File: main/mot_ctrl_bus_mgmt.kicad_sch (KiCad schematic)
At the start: 20 parts, among them Q1401 Q_NMOS_GDS, U1401 74LS08

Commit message: Updates
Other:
- note added: "The motor control is modulated by the power PWM. The low phase is prefered as it will allow the driver charge pump to load. If the feature can be implemented in software, the AND gate can be removed and bypassed."
- note removed: "The motor control is modulated by the power PWM. The low phase is prefered as it will allow the driver charge pump to load. If the feature can be implemented in software, the AND gate can be bypassed."
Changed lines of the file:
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@@
 		)
 	)
-	(text "The motor control is modulated by the power PWM.\nThe low phase is prefered as it will allow the driver charge pump to load.\nIf the feature can be implemented in software, the AND gate can be bypassed."
+	(text "The motor control is modulated by the power PWM.\nThe low phase is prefered as it will allow the driver charge pump to load.\nIf the feature can be implemented in software, the AND gate can be removed and bypassed."
 		(exclude_from_sim no)
 		(at 25.908 71.628 0)
@@
 	(label "MOT_CTRL.BH"
 		(at 147.32 125.73 180)
+		(fields_autoplaced yes)
 		(effects
 			(font
@@
 	(label "MOT_CTRL.CH"
 		(at 147.32 151.13 180)
+		(fields_autoplaced yes)
 		(effects
 			(font
@@
 	(label "MOT_DRIVE.AL"
 		(at 83.82 97.79 180)
+		(fields_autoplaced yes)
 		(effects
 			(font
@@
 	(label "MOT_CTRL.AL"
 		(at 113.03 93.98 0)
+		(fields_autoplaced yes)
 		(effects
 			(font
@@
 	(label "MOT_CTRL.AH"
 		(at 147.32 100.33 180)
+		(fields_autoplaced yes)
 		(effects
 			(font
@@
 	(label "MOT_DRIVE.CL"
 		(at 83.82 148.59 180)
+		(fields_autoplaced yes)
 		(effects
 			(font
@@
 	(label "MOT_DRIVE.BH"
 		(at 158.75 125.73 0)
+		(fields_autoplaced yes)
 		(effects
 			(font
@@
 	(label "MOT_DRIVE.AH"
 		(at 158.75 100.33 0)
+		(fields_autoplaced yes)
 		(effects
 			(font
@@
 	(label "MOT_DRIVE.BL"
 		(at 83.82 123.19 180)
+		(fields_autoplaced yes)
 		(effects
 			(font
@@
 	(label "MOT_CTRL.BL"
 		(at 113.03 119.38 0)
+		(fields_autoplaced yes)
 		(effects
 			(font
@@
 	(label "MOT_DRIVE.CH"
 		(at 158.75 151.13 0)
+		(fields_autoplaced yes)
 		(effects
 			(font
@@
 	(label "MOT_CTRL.CL"
 		(at 113.03 144.78 0)
+		(fields_autoplaced yes)
 		(effects
 			(font

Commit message: Finalize sch and start component mapping
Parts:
- C1401: footprint (none) -> Capacitor_SMD:C_0805_2012Metric
- D1401, D1402, D1403, D1404, D1405, D1406: footprint (none) -> LED_SMD:LED_0805_2012Metric
- JP1101: renamed from JP1204; footprint (none) -> Jumper:SolderJumper-2_P1.3mm_Open_TrianglePad1.0x1.5mm
- JP1103: renamed from JP1201; footprint (none) -> Jumper:SolderJumper-3_P2.0mm_Open_TrianglePad1.0x1.5mm
- JP1104: renamed from JP1202; footprint (none) -> Jumper:SolderJumper-3_P2.0mm_Open_TrianglePad1.0x1.5mm
- JP1402: renamed from JP1502; footprint (none) -> Jumper:SolderJumper-3_P2.0mm_Open_TrianglePad1.0x1.5mm
- R1401, R1402, R1403, R1404, R1405, R1406, R1407: footprint (none) -> Resistor_SMD:R_0805_2012Metric

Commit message: update BOM
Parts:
- U1401: footprint (none) -> Package_DFN_QFN:DHVQFN-14-1EP_2.5x3mm_P0.5mm_EP1x1.5mm; MPN (none) -> 74LVC08ABQ,115
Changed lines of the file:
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@@
 	)
 	(symbol
+		(lib_name "74LS08_2")
 		(lib_id "74xx:74LS08")
 		(at 99.06 100.33 0)
@@
 			)
 		)
-		(property "Footprint" ""
+		(property "Footprint" "Package_DFN_QFN:DHVQFN-14-1EP_2.5x3mm_P0.5mm_EP1x1.5mm"
 			(at 99.06 100.33 0)
 			(effects
@@
 		)
 		(property "Description" "Quad And2"
+			(at 99.06 100.33 0)
+			(effects
+				(font
+					(size 1.27 1.27)
+				)
+				(hide yes)
+			)
+		)
+		(property "MPN" "74LVC08ABQ,115"
 			(at 99.06 100.33 0)
 			(effects
@@
 			)
 		)
-		(property "Footprint" ""
+		(property "Footprint" "Package_DFN_QFN:DHVQFN-14-1EP_2.5x3mm_P0.5mm_EP1x1.5mm"
 			(at 99.06 45.72 0)
 			(effects
@@
 		)
 		(property "Description" "Quad And2"
+			(at 99.06 45.72 0)
+			(effects
+				(font
+					(size 1.27 1.27)
+				)
+				(hide yes)
+			)
+		)
+		(property "MPN" "74LVC08ABQ,115"
 			(at 99.06 45.72 0)
 			(effects
@@
 			)
 		)
-		(property "Footprint" ""
+		(property "Footprint" "Package_DFN_QFN:DHVQFN-14-1EP_2.5x3mm_P0.5mm_EP1x1.5mm"
 			(at 99.06 151.13 0)
 			(effects
@@
 		)
 		(property "Description" "Quad And2"
+			(at 99.06 151.13 0)
+			(effects
+				(font
+					(size 1.27 1.27)
+				)
+				(hide yes)
+			)
+		)
+		(property "MPN" "74LVC08ABQ,115"
 			(at 99.06 151.13 0)
 			(effects
@@
 			)
 		)
-		(property "Footprint" ""
+		(property "Footprint" "Package_DFN_QFN:DHVQFN-14-1EP_2.5x3mm_P0.5mm_EP1x1.5mm"
 			(at 99.06 171.45 0)
 			(effects
@@
 		)
 		(property "Description" "Quad And2"
+			(at 99.06 171.45 0)
+			(effects
+				(font
+					(size 1.27 1.27)
+				)
+				(hide yes)
+			)
+		)
+		(property "MPN" "74LVC08ABQ,115"
 			(at 99.06 171.45 0)
 			(effects
@@
 	)
 	(symbol
+		(lib_name "74LS08_1")
 		(lib_id "74xx:74LS08")
 		(at 99.06 125.73 0)
@@
 			)
 		)
-		(property "Footprint" ""
+		(property "Footprint" "Package_DFN_QFN:DHVQFN-14-1EP_2.5x3mm_P0.5mm_EP1x1.5mm"
 			(at 99.06 125.73 0)
 			(effects
@@
 			(at 99.06 125.73 0)
 			(effects
+				(font
+					(size 1.27 1.27)
+				)
+				(hide yes)
+			)
+		)
+		(property "MPN" "74LVC08ABQ,115"
+			(at 99.06 125.73 0)
+			(effects

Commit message: BOM OK
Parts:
- removed Q1401: Q_NMOS_GDS, symbol Device:Q_NMOS_GDS
- added Q1101: IRLML0030, Package_TO_SOT_SMD:SOT-23, symbol Transistor_FET:IRLML0030
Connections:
- net GNDD: now also Q1101.2 (S)
- net LED_EN: now also Q1101.1 (G)
- net at D1401.1 (K), D1402.1 (K), D1403.1 (K)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: now also Q1101.3 (D)
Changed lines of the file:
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@@
-	)
-	(symbol
-		(lib_id "Device:Q_NMOS_GDS")
-		(at 264.16 76.2 0)
-		(unit 1)
-		(exclude_from_sim no)
-		(in_bom yes)
-		(on_board yes)
-		(dnp no)
-		(fields_autoplaced yes)
-		(property "Reference" "Q1401"
-			(at 270.51 74.9299 0)
-			(effects
-				(font
-					(size 1.27 1.27)
-				)
-				(justify left)
-			)
-		)
-		(property "Value" "Q_NMOS_GDS"
-			(at 270.51 77.4699 0)
-			(effects
-				(font
-					(size 1.27 1.27)
-				)
-				(justify left)
-			)
-		)
-		(property "Footprint" ""
-			(at 269.24 73.66 0)
-			(effects
-				(font
-					(size 1.27 1.27)
-				)
-				(hide yes)
-			)
-		)
-		(property "Datasheet" "~"
-			(at 264.16 76.2 0)
-			(effects
-				(font
-					(size 1.27 1.27)
-				)
-				(hide yes)
-			)
-		)
-		(property "Description" "N-MOSFET transistor, gate/drain/source"
-			(at 264.16 76.2 0)
-			(effects
-				(font
-					(size 1.27 1.27)
-				)
-				(hide yes)
-			)
-		)
-		(pin "2"
-		)
-		(pin "3"
-		)
-		(pin "1"
-		)
-		(instances
-			(project "dsv4"
-				(path "/c07e9297-fde8-4755-803e-d05072cd6096/0865f076-bf0e-442f-8617-d4097538e68b/e313533d-7862-466d-aec4-d9675212cabe"
-					(reference "Q1401")
-					(unit 1)
-				)
-				(path "/c07e9297-fde8-4755-803e-d05072cd6096/0865f076-bf0e-442f-8617-d4097538e68b/2d15f287-a464-4822-9e76-d4ca4cb9f82a"
-					(reference "Q1101")
-					(unit 1)
-				)
-			)
-		)
 	)
 	(symbol
@@
 					(unit 1)
 				)
+			)
+		)
+	)
+	(symbol
+		(lib_id "Transistor_FET:IRLML0030")
+		(at 264.16 76.2 0)
+		(unit 1)
+		(exclude_from_sim no)
+		(in_bom yes)
+		(on_board yes)
+		(dnp no)
+		(fields_autoplaced yes)
+		(property "Reference" "Q1101"
+			(at 270.51 74.9299 0)
+			(effects
+				(font
+					(size 1.27 1.27)
+				)
+				(justify left)
+			)
+		)
+		(property "Value" "IRLML0030"
+			(at 270.51 77.4699 0)
+			(effects
+				(font
+					(size 1.27 1.27)
+				)
+				(justify left)
+			)
+		)
+		(property "Footprint" "Package_TO_SOT_SMD:SOT-23"
+			(at 269.24 78.105 0)
+			(effects
+				(font
+					(size 1.27 1.27)
+					(italic yes)
+				)
+				(justify left)
+				(hide yes)
+			)
+		)
+		(property "Datasheet" "https://www.infineon.com/dgdl/irlml0030pbf.pdf?fileId=5546d462533600a401535664773825df"
+			(at 269.24 80.01 0)
+			(effects
+				(font
+					(size 1.27 1.27)
+				)
+				(justify left)
+				(hide yes)
+			)
+		)
+		(property "Description" "5.3A Id, 30V Vds, 27mOhm Rds, N-Channel HEXFET Power MOSFET, SOT-23"
+			(at 264.16 76.2 0)
+			(effects
+				(font
+					(size 1.27 1.27)
+				)
+				(hide yes)
+			)
+		)
+		(pin "1"
+		)
+		(pin "3"
+		)
+		(pin "2"
+		)
+		(instances
+			(project "dsv4"
+				(path "/c07e9297-fde8-4755-803e-d05072cd6096/0865f076-bf0e-442f-8617-d4097538e68b/2d15f287-a464-4822-9e76-d4ca4cb9f82a"
+					(reference "Q1101")
+					(unit 1)
+				)
+				(path "/c07e9297-fde8-4755-803e-d05072cd6096/0865f076-bf0e-442f-8617-d4097538e68b/e313533d-7862-466d-aec4-d9675212cabe"
+					(reference "Q1401")
+					(unit 1)
+				)

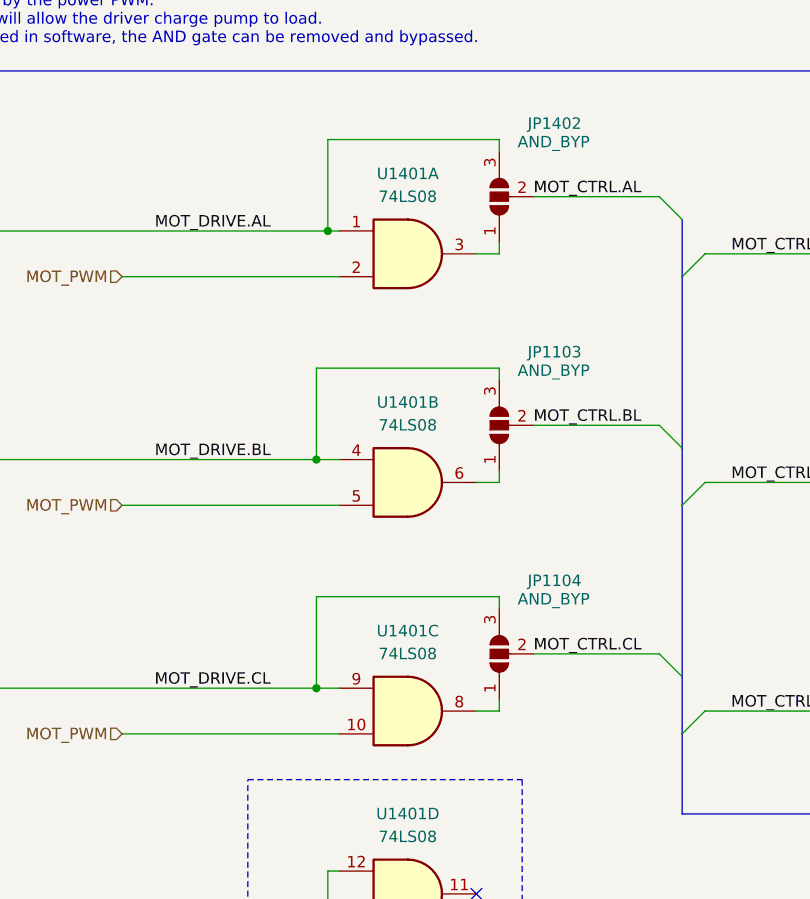
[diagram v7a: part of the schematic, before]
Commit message: Power routed
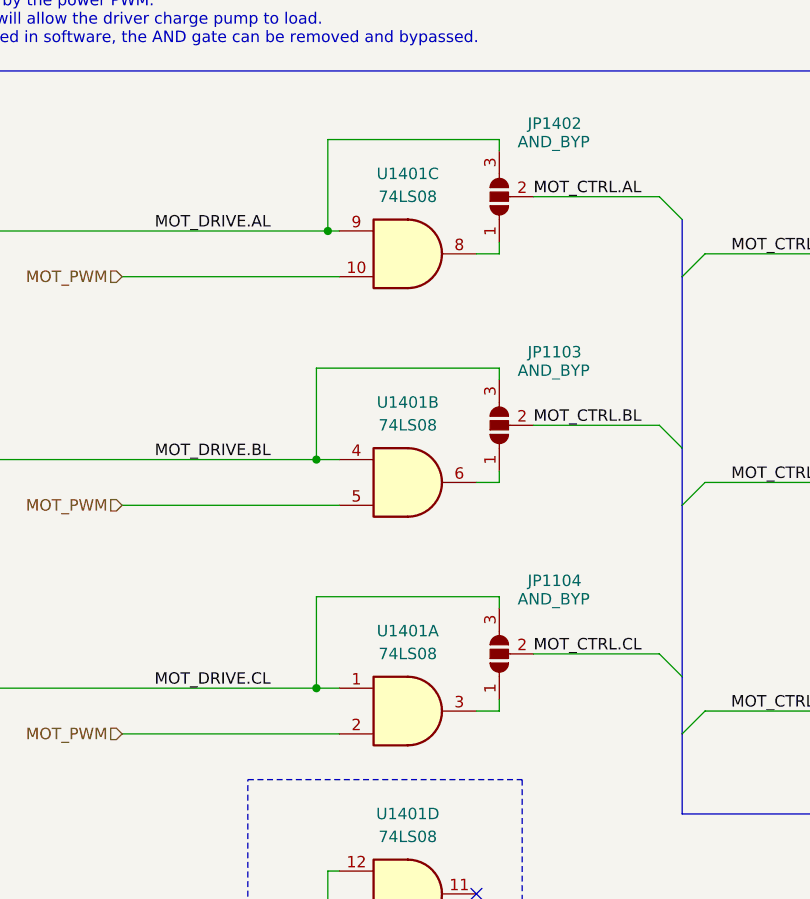
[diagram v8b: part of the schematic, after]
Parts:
- U1401: footprint Package_DFN_QFN:DHVQFN-14-1EP_2.5x3mm_P0.5mm_EP1x1.5mm -> Package_SO:TSSOP-14_4.4x5mm_P0.65mm
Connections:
- net MOT_DRIVE.AL: now also U1401.9; no longer U1401.1
- net MOT_DRIVE.CL: now also U1401.1; no longer U1401.9
- net at U1401.3: now also JP1104.1 (A); no longer JP1402.1 (A)
- net at U1401.8: now also JP1402.1 (A); no longer JP1104.1 (A)
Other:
- moved on the sheet: U1401A, U1401C
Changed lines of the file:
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@@
 		(comment 1 "Defis solaires 2024")
 	)
+	(rectangle
+		(start 81.28 158.75)
+		(end 111.76 186.69)
+		(stroke
+			(width 0)
+			(type dash)
+		)
+		(fill
+			(type none)
+		)
+	)
+	(text "Any high value to avoid floating gate\nwhile not wasting power."
+		(exclude_from_sim no)
+		(at 247.904 82.55 0)
+		(effects
+			(font
+				(size 1.27 1.27)
+			)
+			(justify right bottom)
+		)
+	)
+	(text "Unused"
+		(exclude_from_sim no)
+		(at 111.252 186.182 0)
+		(effects
+			(font
+				(size 1.27 1.27)
+			)
+			(justify right bottom)
+		)
+	)
+	(text "The motor control is modulated by the power PWM.\nThe low phase is prefered as it will allow the driver charge pump to load.\nIf the feature can be implemented in software, the AND gate can be removed and bypassed."
+		(exclude_from_sim no)
+		(at 25.908 71.628 0)
+		(effects
+			(font
+				(size 1.27 1.27)
+			)
+			(justify left top)
+		)
+	)
 	(junction
 		(at 50.8 80.01)
@@
 		)
 	)
-	(rectangle
-		(start 81.28 158.75)
-		(end 111.76 186.69)
-		(stroke
-			(width 0)
-			(type dash)
-		)
-		(fill
-			(type none)
-		)
-	)
-	(text "Any high value to avoid floating gate\nwhile not wasting power."
-		(exclude_from_sim no)
-		(at 247.904 82.55 0)
-		(effects
-			(font
-				(size 1.27 1.27)
-			)
-			(justify right bottom)
-		)
-	)
-	(text "Unused"
-		(exclude_from_sim no)
-		(at 111.252 186.182 0)
-		(effects
-			(font
-				(size 1.27 1.27)
-			)
-			(justify right bottom)
-		)
-	)
-	(text "The motor control is modulated by the power PWM.\nThe low phase is prefered as it will allow the driver charge pump to load.\nIf the feature can be implemented in software, the AND gate can be removed and bypassed."
-		(exclude_from_sim no)
-		(at 25.908 71.628 0)
-		(effects
-			(font
-				(size 1.27 1.27)
-			)
-			(justify left top)
-		)
-	)
 	(label "MOT_CTRL.BH"
 		(at 147.32 125.73 180)
@@
 		(lib_name "74LS08_2")
 		(lib_id "74xx:74LS08")
-		(at 99.06 100.33 0)
+		(at 99.06 151.13 0)
 		(unit 1)
 		(exclude_from_sim no)
@@
 		(fields_autoplaced yes)
 		(property "Reference" "U1401"
-			(at 99.0517 91.44 0)
+			(at 99.0517 142.24 0)
 			(effects
 				(font
@@
 		)
 		(property "Value" "74LS08"
-			(at 99.0517 93.98 0)
+			(at 99.0517 144.78 0)
 			(effects
 				(font
@@
 			)
 		)
-		(property "Footprint" "Package_DFN_QFN:DHVQFN-14-1EP_2.5x3mm_P0.5mm_EP1x1.5mm"
-			(at 99.06 100.33 0)
+		(property "Footprint" "Package_SO:TSSOP-14_4.4x5mm_P0.65mm"
+			(at 99.06 151.13 0)
 			(effects
 				(font
@@
 		)
 		(property "Datasheet" "http://www.ti.com/lit/gpn/sn74LS08"
-			(at 99.06 100.33 0)
+			(at 99.06 151.13 0)
 			(effects
 				(font
@@
 		)
 		(property "Description" "Quad And2"
-			(at 99.06 100.33 0)
+			(at 99.06 151.13 0)
 			(effects
 				(font
@@
 		)
 		(property "MPN" "74LVC08ABQ,115"
-			(at 99.06 100.33 0)
+			(at 99.06 151.13 0)
 			(effects
 				(font
@@
 			)
 		)
-		(property "Footprint" "Package_DFN_QFN:DHVQFN-14-1EP_2.5x3mm_P0.5mm_EP1x1.5mm"
+		(property "Footprint" "Package_SO:TSSOP-14_4.4x5mm_P0.65mm"
 			(at 99.06 45.72 0)
 			(effects
@@
 	(symbol
 		(lib_id "74xx:74LS08")
-		(at 99.06 151.13 0)
+		(at 99.06 100.33 0)
 		(unit 3)
 		(exclude_from_sim no)
@@
 		(fields_autoplaced yes)
 		(property "Reference" "U1401"
-			(at 99.0517 142.24 0)
+			(at 99.0517 91.44 0)
 			(effects
 				(font
@@
 		)
 		(property "Value" "74LS08"
-			(at 99.0517 144.78 0)
+			(at 99.0517 93.98 0)
 			(effects
 				(font
@@
 			)
 		)
-		(property "Footprint" "Package_DFN_QFN:DHVQFN-14-1EP_2.5x3mm_P0.5mm_EP1x1.5mm"
-			(at 99.06 151.13 0)
+		(property "Footprint" "Package_SO:TSSOP-14_4.4x5mm_P0.65mm"
+			(at 99.06 100.33 0)
 			(effects
 				(font
@@
 		)
 		(property "Datasheet" "http://www.ti.com/lit/gpn/sn74LS08"
-			(at 99.06 151.13 0)
+			(at 99.06 100.33 0)
 			(effects
 				(font
@@
 		)
 		(property "Description" "Quad And2"
-			(at 99.06 151.13 0)
+			(at 99.06 100.33 0)
 			(effects
 				(font
@@
 		)
 		(property "MPN" "74LVC08ABQ,115"
-			(at 99.06 151.13 0)
+			(at 99.06 100.33 0)
 			(effects
 				(font
@@
 			)
 		)
-		(property "Footprint" "Package_DFN_QFN:DHVQFN-14-1EP_2.5x3mm_P0.5mm_EP1x1.5mm"
+		(property "Footprint" "Package_SO:TSSOP-14_4.4x5mm_P0.65mm"
 			(at 99.06 171.45 0)
 			(effects
@@
 			)
 		)
-		(property "Footprint" "Package_DFN_QFN:DHVQFN-14-1EP_2.5x3mm_P0.5mm_EP1x1.5mm"
+		(property "Footprint" "Package_SO:TSSOP-14_4.4x5mm_P0.65mm"
 			(at 99.06 125.73 0)
 			(effects
